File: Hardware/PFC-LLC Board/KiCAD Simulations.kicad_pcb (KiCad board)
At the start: 2 copper layers, 163.3 x 149.9 mm, 119 parts, among them J1 1792229, J2 Conn_01x02_Female, J3 1792229, J4 1792229, J5 Conn_01x02_Female, J6 1792229, Q1 C2M0160120D, U1 UCC28180DR, U1LLC1 UCC256403DDBR, U2LLC1 UCC24624DT

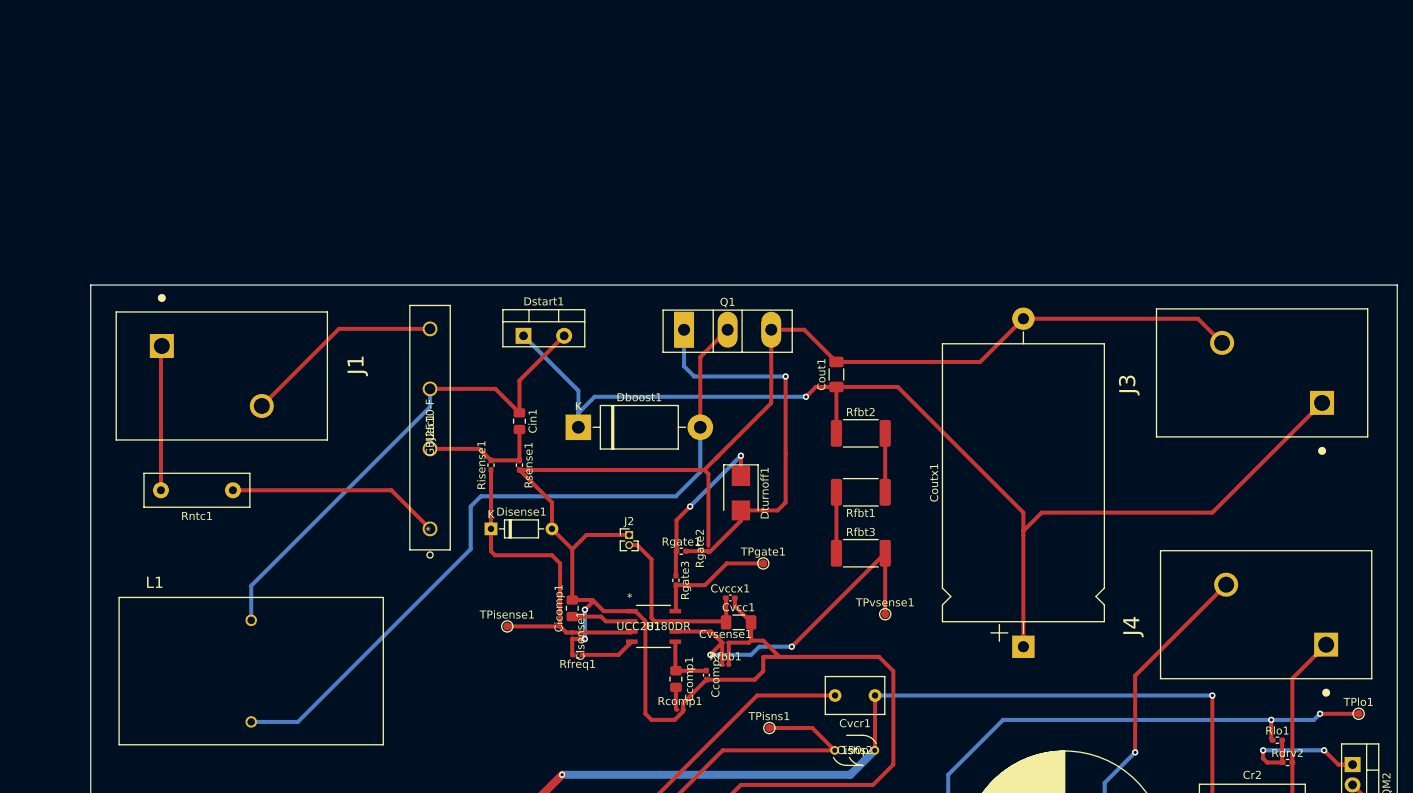
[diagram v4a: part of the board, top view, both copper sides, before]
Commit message: PFC footprints updated
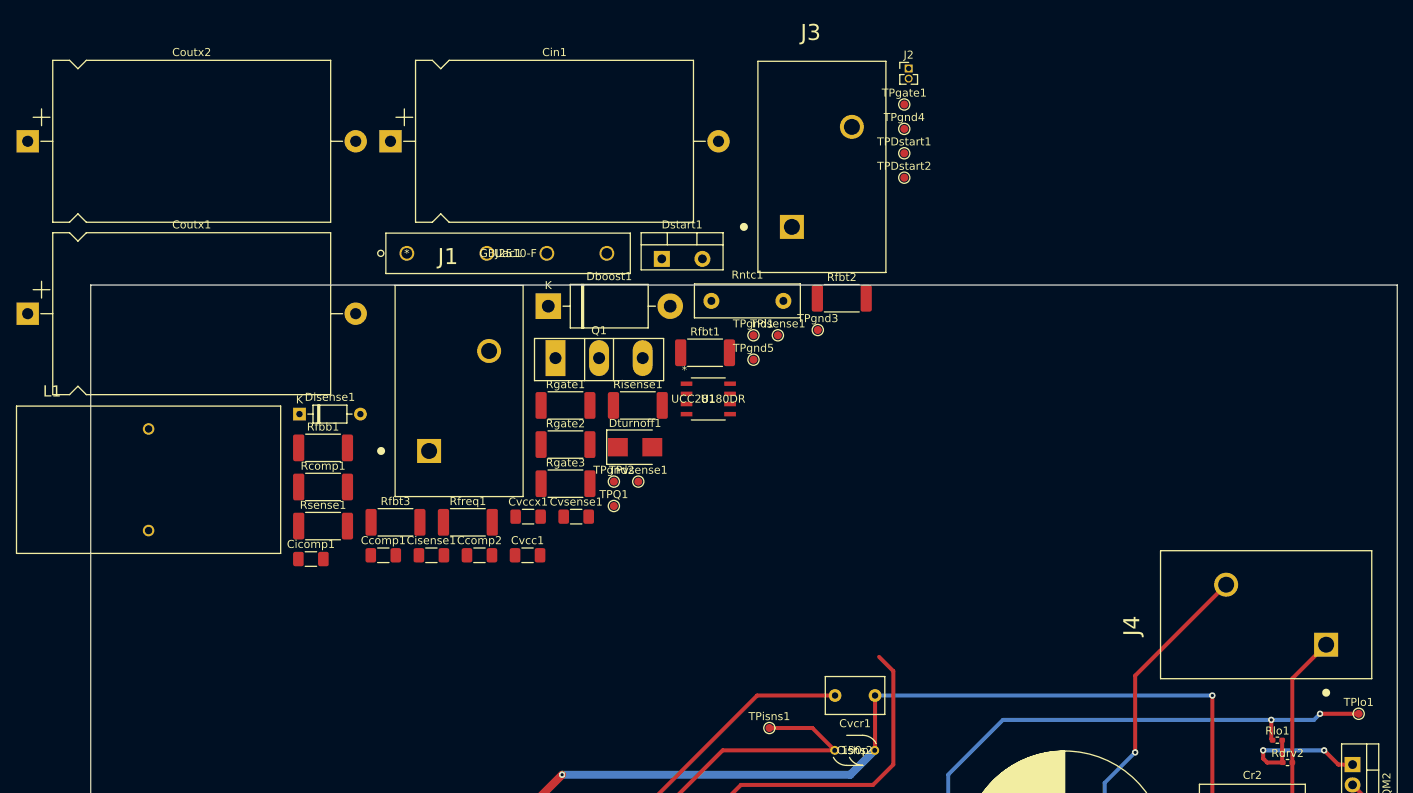
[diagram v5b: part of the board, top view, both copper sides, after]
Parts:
- removed Cout1: 13.585m, Capacitor_SMD:C_1206_3216Metric_Pad1.33x1.80mm_HandSolder
- added Coutx2: 100n, Capacitor_THT:CP_Axial_L34.5mm_D20.0mm_P41.00mm_Horizontal, F.Cu at (42.9, -2.47)
- added TPDstart1: TestPoint Dstart, TestPoint:TestPoint_Pad_D1.0mm, F.Cu at (152.5, -0.97)
- added TPDstart2: TestPoint Dstart2, TestPoint:TestPoint_Pad_D1.0mm, F.Cu at (152.5, 2.08)
- added TPQ1: TestPoint Q1, TestPoint:TestPoint_Pad_D1.0mm, F.Cu at (116.2, 43.1)
- added TPgnd1: TestPoint GND, TestPoint:TestPoint_Pad_D1.0mm, F.Cu at (133.6, 21.8)
- added TPgnd2: TestPoint GND, TestPoint:TestPoint_Pad_D1.0mm, F.Cu at (116.2, 40.1)
- added TPgnd3: TestPoint GND, TestPoint:TestPoint_Pad_D1.0mm, F.Cu at (141.7, 21.1)
- added TPgnd4: TestPoint GND, TestPoint:TestPoint_Pad_D1.0mm, F.Cu at (152.5, -4.02)
- added TPgnd5: TestPoint GND Q1, TestPoint:TestPoint_Pad_D1.0mm, F.Cu at (133.6, 24.8)
- Ccomp1, Cicomp1: footprint Capacitor_SMD:C_0805_2012Metric_Pad1.18x1.45mm_HandSolder -> Capacitor_SMD:C_1206_3216Metric_Pad1.33x1.80mm_HandSolder
- Ccomp2, Cvccx1: footprint Capacitor_SMD:C_0402_1005Metric_Pad0.74x0.62mm_HandSolder -> Capacitor_SMD:C_1206_3216Metric_Pad1.33x1.80mm_HandSolder
- Cin1: value 10n -> 100n; footprint Capacitor_SMD:C_0805_2012Metric_Pad1.18x1.45mm_HandSolder -> Capacitor_THT:CP_Axial_L34.5mm_D20.0mm_P41.00mm_Horizontal
- Cisense1, Cvsense1: footprint Capacitor_SMD:C_0201_0603Metric_Pad0.64x0.40mm_HandSolder -> Capacitor_SMD:C_1206_3216Metric_Pad1.33x1.80mm_HandSolder
- Rcomp1, Rfbb1, Rgate2: footprint Resistor_SMD:R_0201_0603Metric_Pad0.64x0.40mm_HandSolder -> Resistor_SMD:R_2512_6332Metric_Pad1.40x3.35mm_HandSolder
- Rfreq1, Rgate3, Risense1, Rsense1: footprint Resistor_SMD:R_0402_1005Metric_Pad0.72x0.64mm_HandSolder -> Resistor_SMD:R_2512_6332Metric_Pad1.40x3.35mm_HandSolder
- Rgate1: value 1.07 -> 1.00; footprint Resistor_SMD:R_0402_1005Metric_Pad0.72x0.64mm_HandSolder -> Resistor_SMD:R_2512_6332Metric_Pad1.40x3.35mm_HandSolder
- TPgate1: value TestPoint -> TestPoint Gate Pin
- moved Coutx1 131.2 mm to (42.9, 19.1), turned to 0 degrees
- moved J3 69.8 mm to (138.5, 8.23), turned to 0 degrees
- moved J2 68.0 mm to (153.0, -11.6)
- moved Rntc1 64.3 mm to (128.4, 17.5), turned to 0 degrees
- moved TPgate1 60.0 mm to (152.5, -7.07)
- moved Rfbt3 58.3 mm to (88.9, 45.2)
- moved Rfbb1 57.2 mm to (79.8, 35.8)
- moved Rcomp1 52.6 mm to (79.8, 40.7)
- moved TPisense1 49.7 mm to (136.7, 21.8)
- moved Ccomp1 39.7 mm to (87.4, 49.3), turned to 0 degrees
- moved Cin1 38.5 mm to (88.3, -2.47), turned to 0 degrees
- moved J1 35.9 mm to (93.1, 36.2), turned to 0 degrees
- moved TPvsense1 35.0 mm to (119.2, 40.1)
- moved Uac1 34.6 mm to (90.3, 11.5), turned to 0 degrees
- moved Cicomp1 33.2 mm to (78.3, 49.7), turned to 0 degrees
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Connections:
- Rgate1 pad 1: Net-(Dturnoff1-Pad1) -> Net-(Rgate1-Pad1)
- Rgate3 pad 2: Net-(Rgate3-Pad2) -> Net-(Rgate1-Pad1)
- TPgate1 pad 1: Net-(Rgate3-Pad2) -> Net-(Rgate1-Pad1)
- U1 pad 8: Net-(Rgate3-Pad2) -> Net-(Rgate1-Pad1)
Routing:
- net GND: track 713.3 -> 489.2 mm, vias 4 -> 2
- net Net-(Coutx1-Pad1): track 146.1 -> 0.00 mm, vias 1 -> 0
- net Net-(Dboost1-Pad2): track 91.4 -> 0.00 mm
- net Net-(Cin1-Pad1): track 62.6 -> 0.00 mm
- net Net-(Dturnoff1-Pad2): track 49.3 -> 0.00 mm, vias 1 -> 0
- net Net-(Cvsense1-Pad1): track 46.1 -> 0.00 mm, vias 2 -> 0
- net Net-(Cisense1-Pad1): track 43.2 -> 0.00 mm
- net Net-(Rntc1-Pad1): track 26.6 -> 0.00 mm
- net Net-(J1-Pad2): track 25.0 -> 0.00 mm
- net Net-(Cvcc1-Pad1): track 23.5 -> 0.00 mm
- net Net-(Dturnoff1-Pad1): track 20.9 -> 0.00 mm, vias 2 -> 0
- net Net-(J1-Pad1): track 18.1 -> 0.00 mm
- net Net-(Cin1-Pad2): track 15.6 -> 0.00 mm
- net Net-(Rgate3-Pad2): track 15.3 -> 0.00 mm
- net Net-(Cicomp1-Pad1): track 7.68 -> 0.00 mm
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
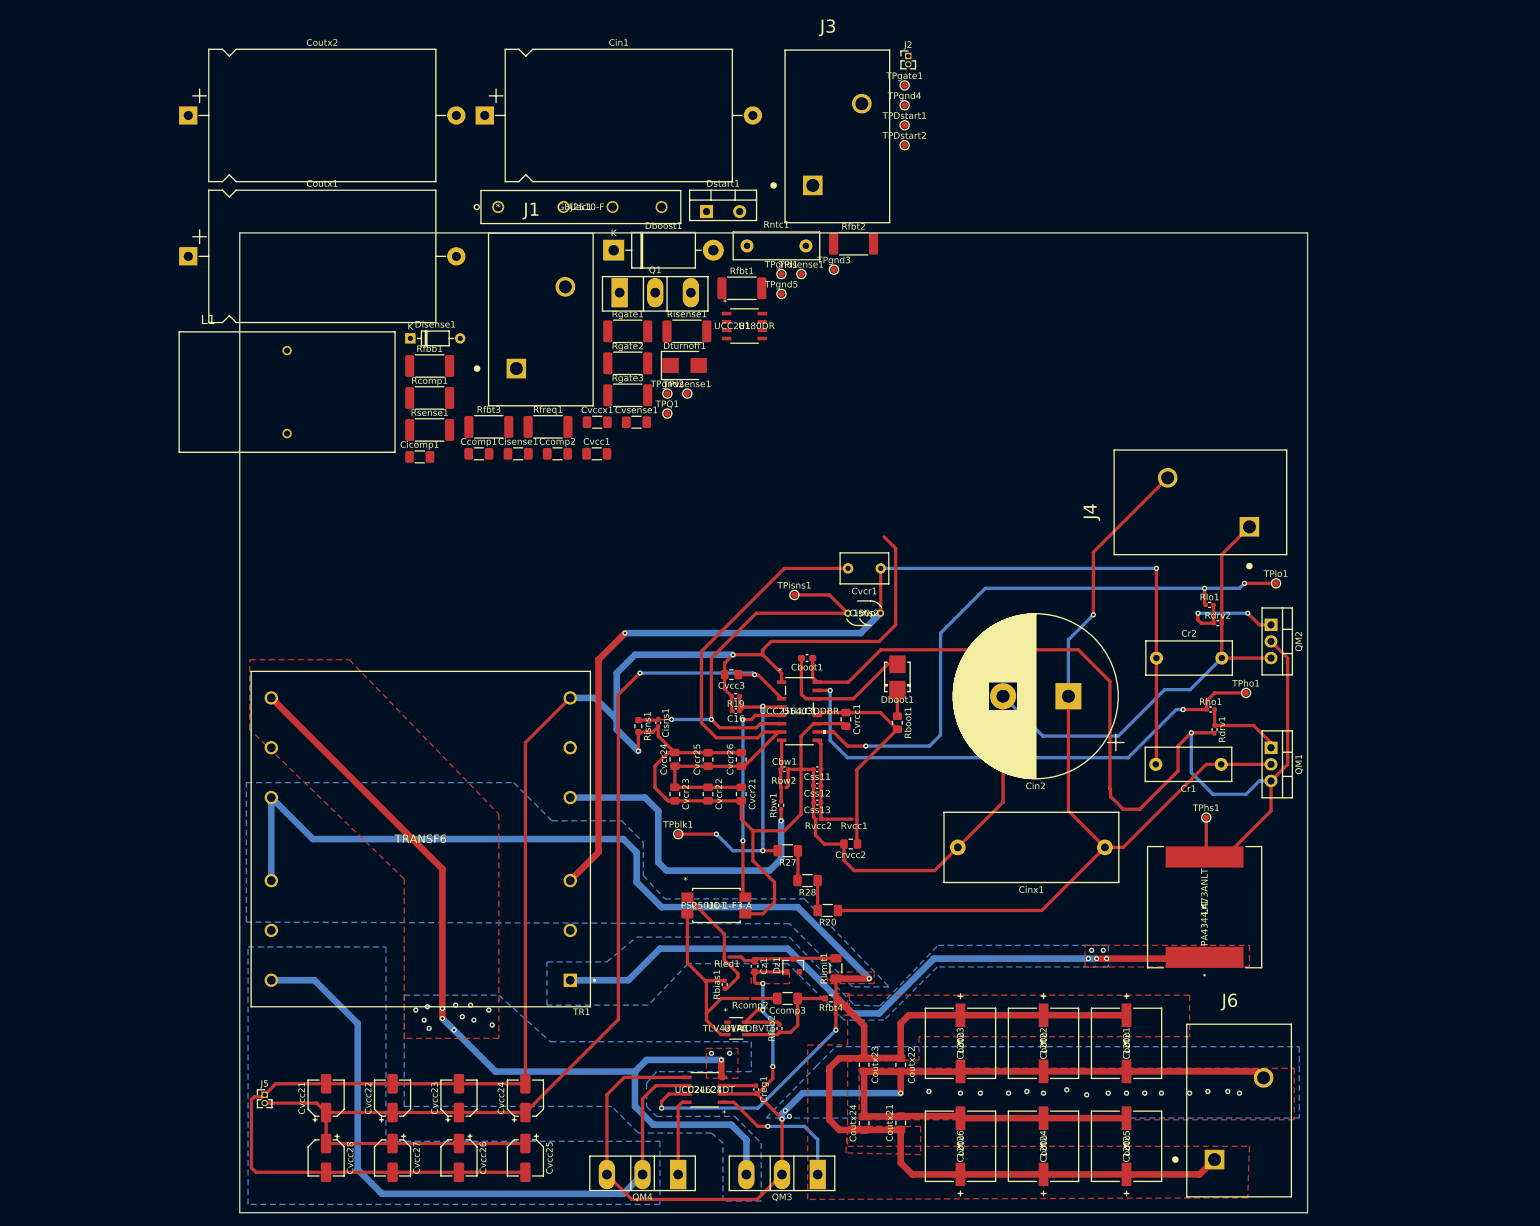
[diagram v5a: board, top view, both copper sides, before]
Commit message: new PFC Board/Design
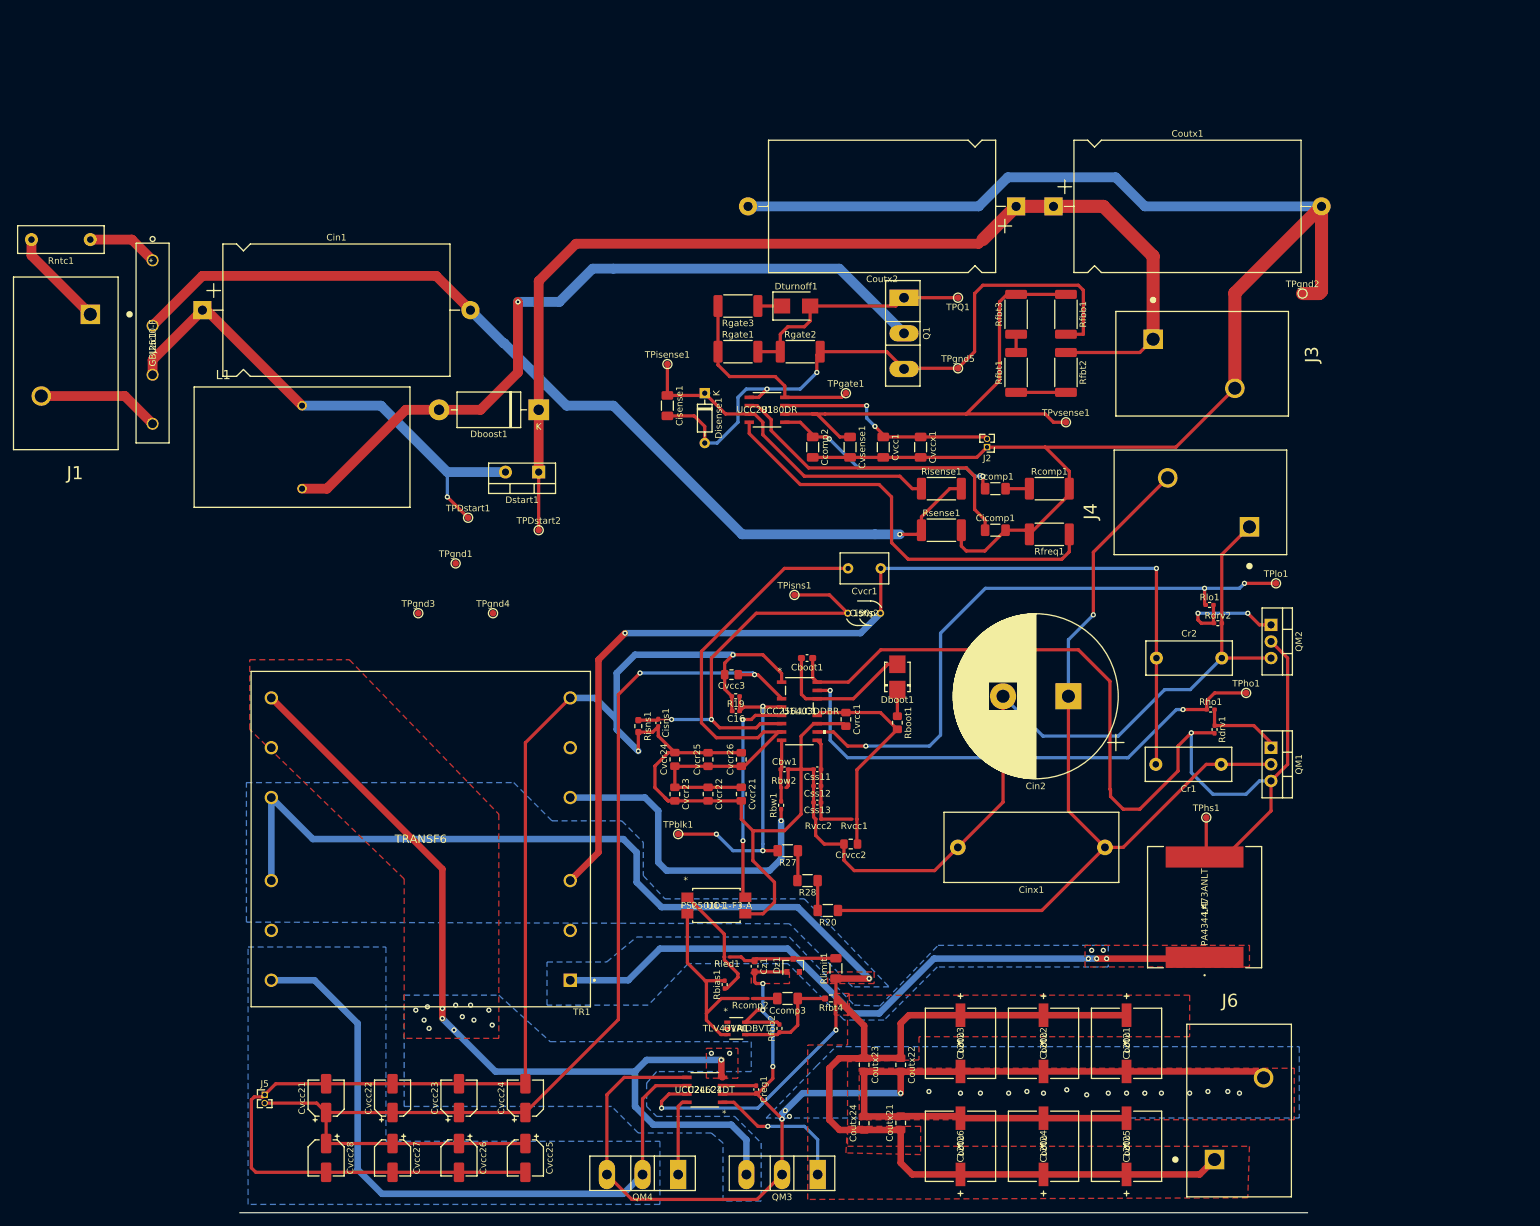
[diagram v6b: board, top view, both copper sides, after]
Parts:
- J3: value 1792229 -> PFC OUT
- J4: value 1792229 -> LLC IN
- TPQ1: value TestPoint Q1 -> TP Q1
- TPgnd5: value TestPoint GND Q1 -> TP GND Q1
- moved Coutx1 132.6 mm to (175.3, 11.4)
- moved Coutx2 127.4 mm to (169.5, 11.4), turned to 180 degrees
- moved Rntc1 100.5 mm to (27.9, 16.5), turned to 180 degrees
- moved TPgnd4 100.0 mm to (89.5, 73.7)
- moved TPgnd2 98.4 mm to (213.4, 24.8)
- moved Rfbb1 97.6 mm to (177.2, 27.9), turned to 270 degrees
- moved Rcomp1 95.8 mm to (174.6, 54.6)
- moved TPDstart1 89.8 mm to (85.7, 59.1)
- moved Cicomp1 88.8 mm to (166.4, 61.0)
- moved TPgnd3 82.5 mm to (78.1, 73.7)
- moved Rfbt3 82.5 mm to (169.5, 27.9), turned to 90 degrees
- moved TPDstart2 81.2 mm to (96.5, 61.0)
- moved Rsense1 79.8 mm to (158.1, 61.0)
- moved Ccomp1 79.2 mm to (166.4, 54.6)
- moved Rfreq1 78.4 mm to (174.6, 61.6), turned to 180 degrees
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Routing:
- net GND: track 489.2 -> 795.5 mm, vias 2 -> 4
- net Net-(Coutx1-Pad1): track 0.00 -> 166.8 mm
- net Net-(Cin1-Pad2): track 0.00 -> 147.3 mm, vias 0 -> 1
- net Net-(Dboost1-Pad2): track 0.00 -> 116.4 mm, vias 0 -> 1
- net Net-(Cvsense1-Pad1): track 0.00 -> 80.8 mm
- net Net-(Cin1-Pad1): track 0.00 -> 77.9 mm, vias 0 -> 1
- net Net-(Rfreq1-Pad1): track 0.00 -> 65.9 mm
- net Net-(Cisense1-Pad1): track 0.00 -> 52.4 mm
- net Net-(Cicomp1-Pad1): track 0.00 -> 48.9 mm
- net Net-(Dturnoff1-Pad2): track 0.00 -> 36.9 mm
- net Net-(Ccomp1-Pad1): track 0.00 -> 36.4 mm, vias 0 -> 2
- net Net-(Cvcc1-Pad1): track 0.00 -> 34.4 mm, vias 0 -> 2
- net Net-(Rgate1-Pad1): track 0.00 -> 31.9 mm
- net Net-(J1-Pad2): track 0.00 -> 18.8 mm
- net Net-(J1-Pad1): track 0.00 -> 15.2 mm
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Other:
- board outline removed
